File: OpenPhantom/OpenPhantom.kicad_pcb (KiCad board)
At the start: 2 copper layers, 175 x 175 mm, 110 parts, among them J1 Barrel_Jack, J2 Video, J3 Audio, Q1 BC548, Q2 BD136, Q3 BC557, Q4 BC548, SW1 POWER, SW2 RESET, U1 UM6116 VRAM, U10 74HC368, U11 74HC368, U2 UM6116 WRAM, U3 74HC04, U4 UA6547_CPU, U5 4013, U6 UA6548_PPU, U7 74HC139, U8 74LS373, U9 LM7805, Y1 21.453366 MHz

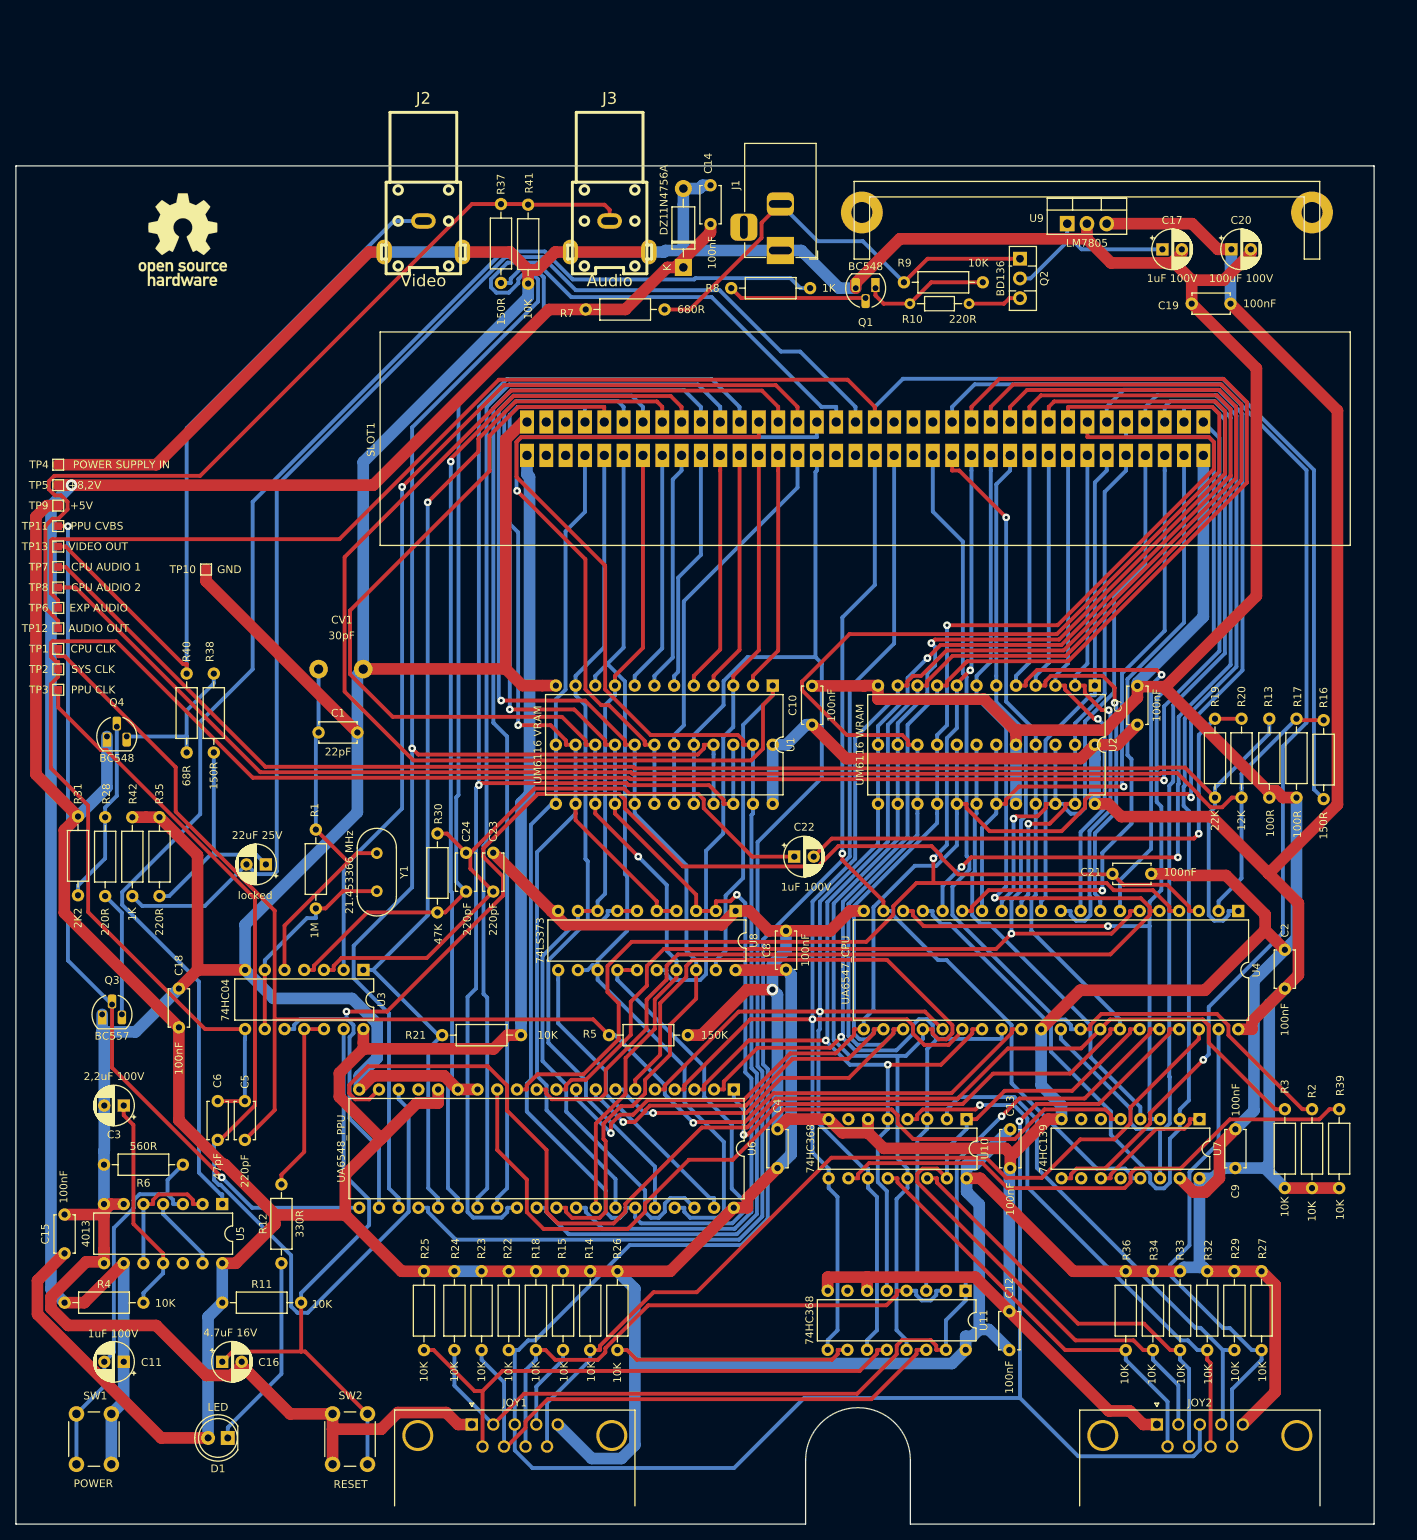
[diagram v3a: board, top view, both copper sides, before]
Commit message: Fixed Routes
Power route fix.
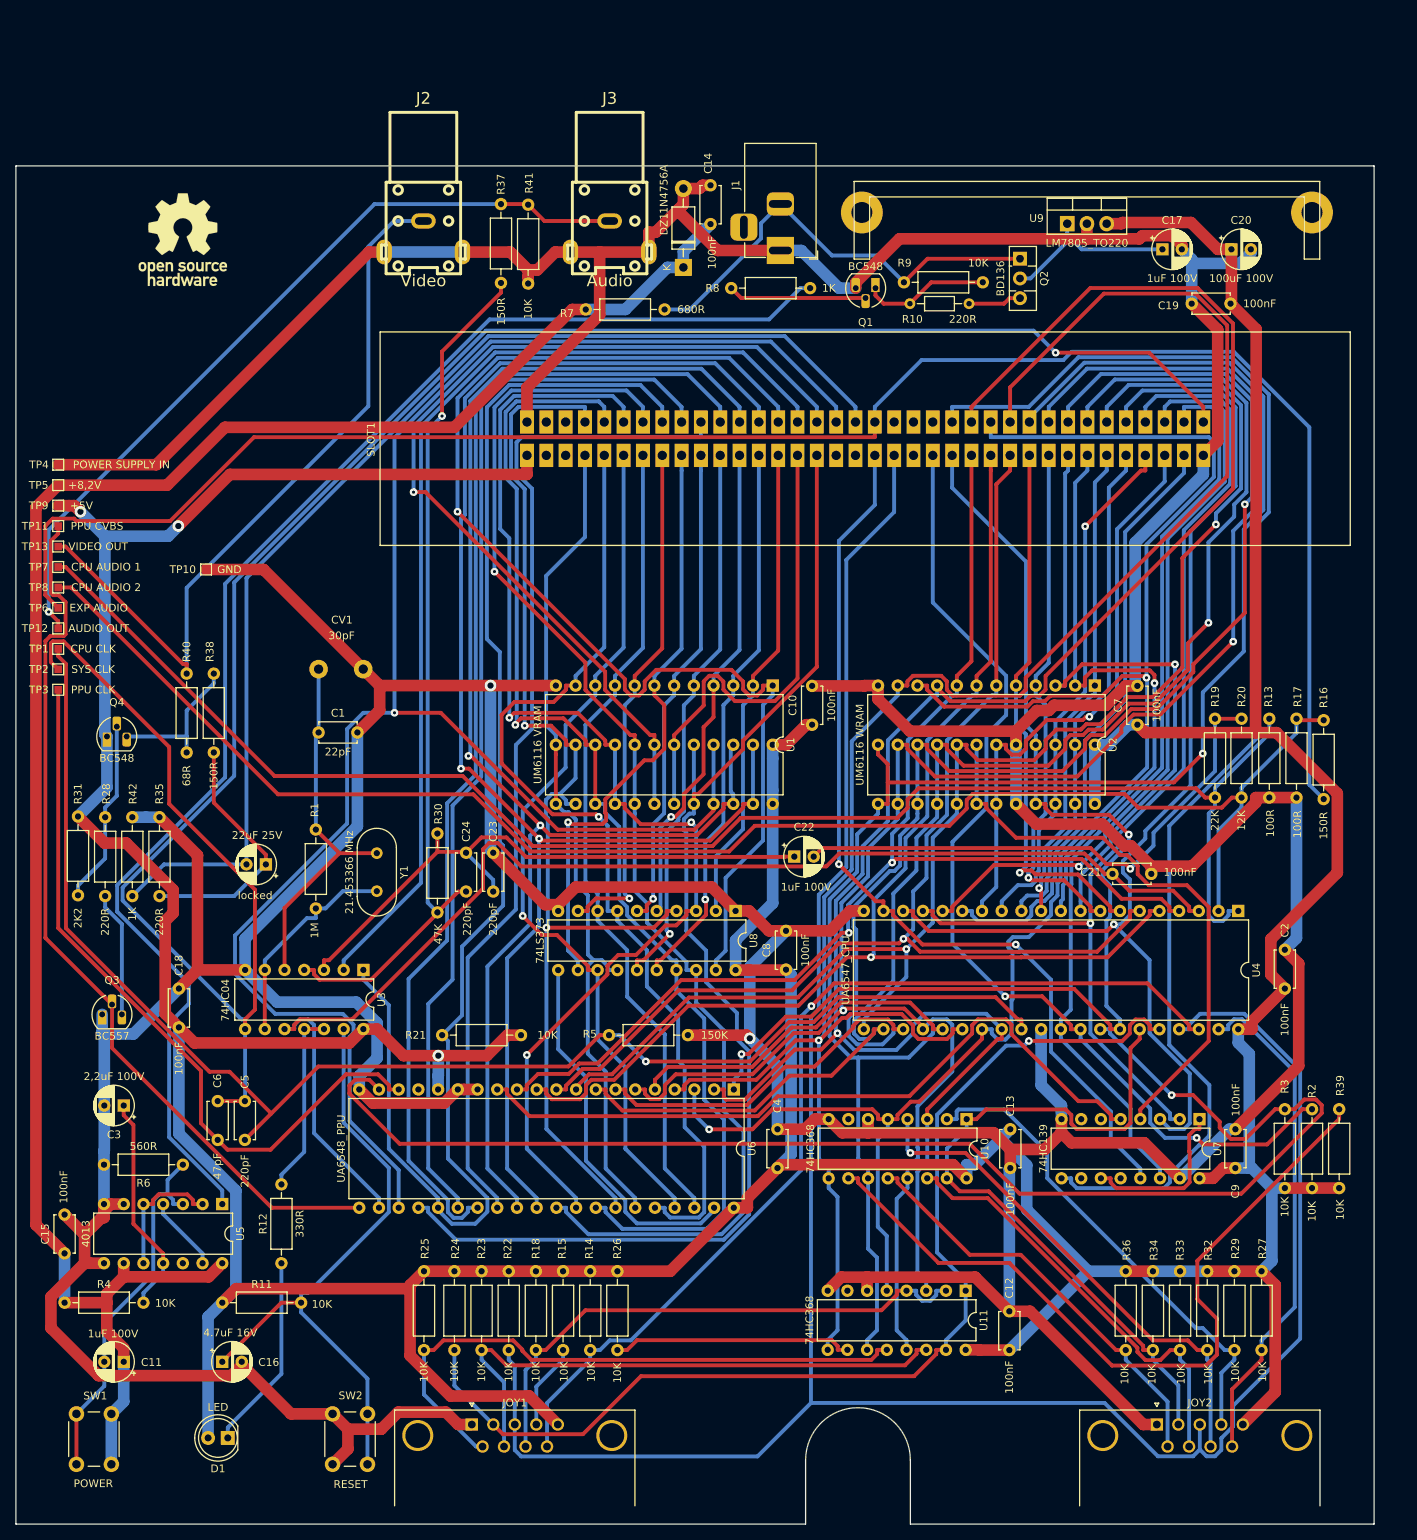
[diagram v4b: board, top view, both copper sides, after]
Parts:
- U9: value LM7805 -> LM7805_TO220
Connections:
- C15 pad 1: /VCC -> /+8,2V
- U5 pad 14: /VCC -> /+8,2V
- U8 pad 12: /PPU-D1 -> /PPU-A1
- U8 pad 15: /PPU-D3 -> /PPU-A3
- U8 pad 2: /PPU-D6 -> /PPU-A6
- U8 pad 5: /PPU-D4 -> /PPU-A4
- U8 pad 6: /PPU-D2 -> /PPU-A2
- U8 pad 9: /PPU-D0 -> /PPU-A0
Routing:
- net /VCC: track 899.1 -> 765.1 mm, vias 0 -> 3
- net /GND: track 1118.3 -> 1007.0 mm, vias 1 -> 2
- net /PPU-D3: track 166.9 -> 108.6 mm
- net /PPU-A1: track 31.1 -> 77.6 mm, vias 0 -> 1
- net /CPU-D3: track 228.0 -> 269.6 mm, vias 2 -> 1
- net /PPU-A13: track 139.0 -> 179.7 mm, vias 1 -> 0
- net /PPU-A3: track 31.1 -> 71.6 mm, vias 0 -> 1
- net /PPU-CLK: track 134.2 -> 95.5 mm
- net /PPU-A0: track 31.1 -> 67.0 mm, vias 0 -> 1
- net /PPU-A7: track 191.5 -> 158.4 mm, vias 0 -> 1
- net /PPU-A4: track 31.0 -> 63.4 mm, vias 0 -> 1
- net /PPU-A2: track 31.1 -> 62.8 mm, vias 0 -> 1
- net /PPU-A6: track 31.0 -> 62.0 mm
- net /CPU-A13: track 169.9 -> 141.1 mm, vias 0 -> 1
- net /4017-D2: track 70.6 -> 98.6 mm
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
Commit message: RCA Plug fix
Fixed RCA plug pinout
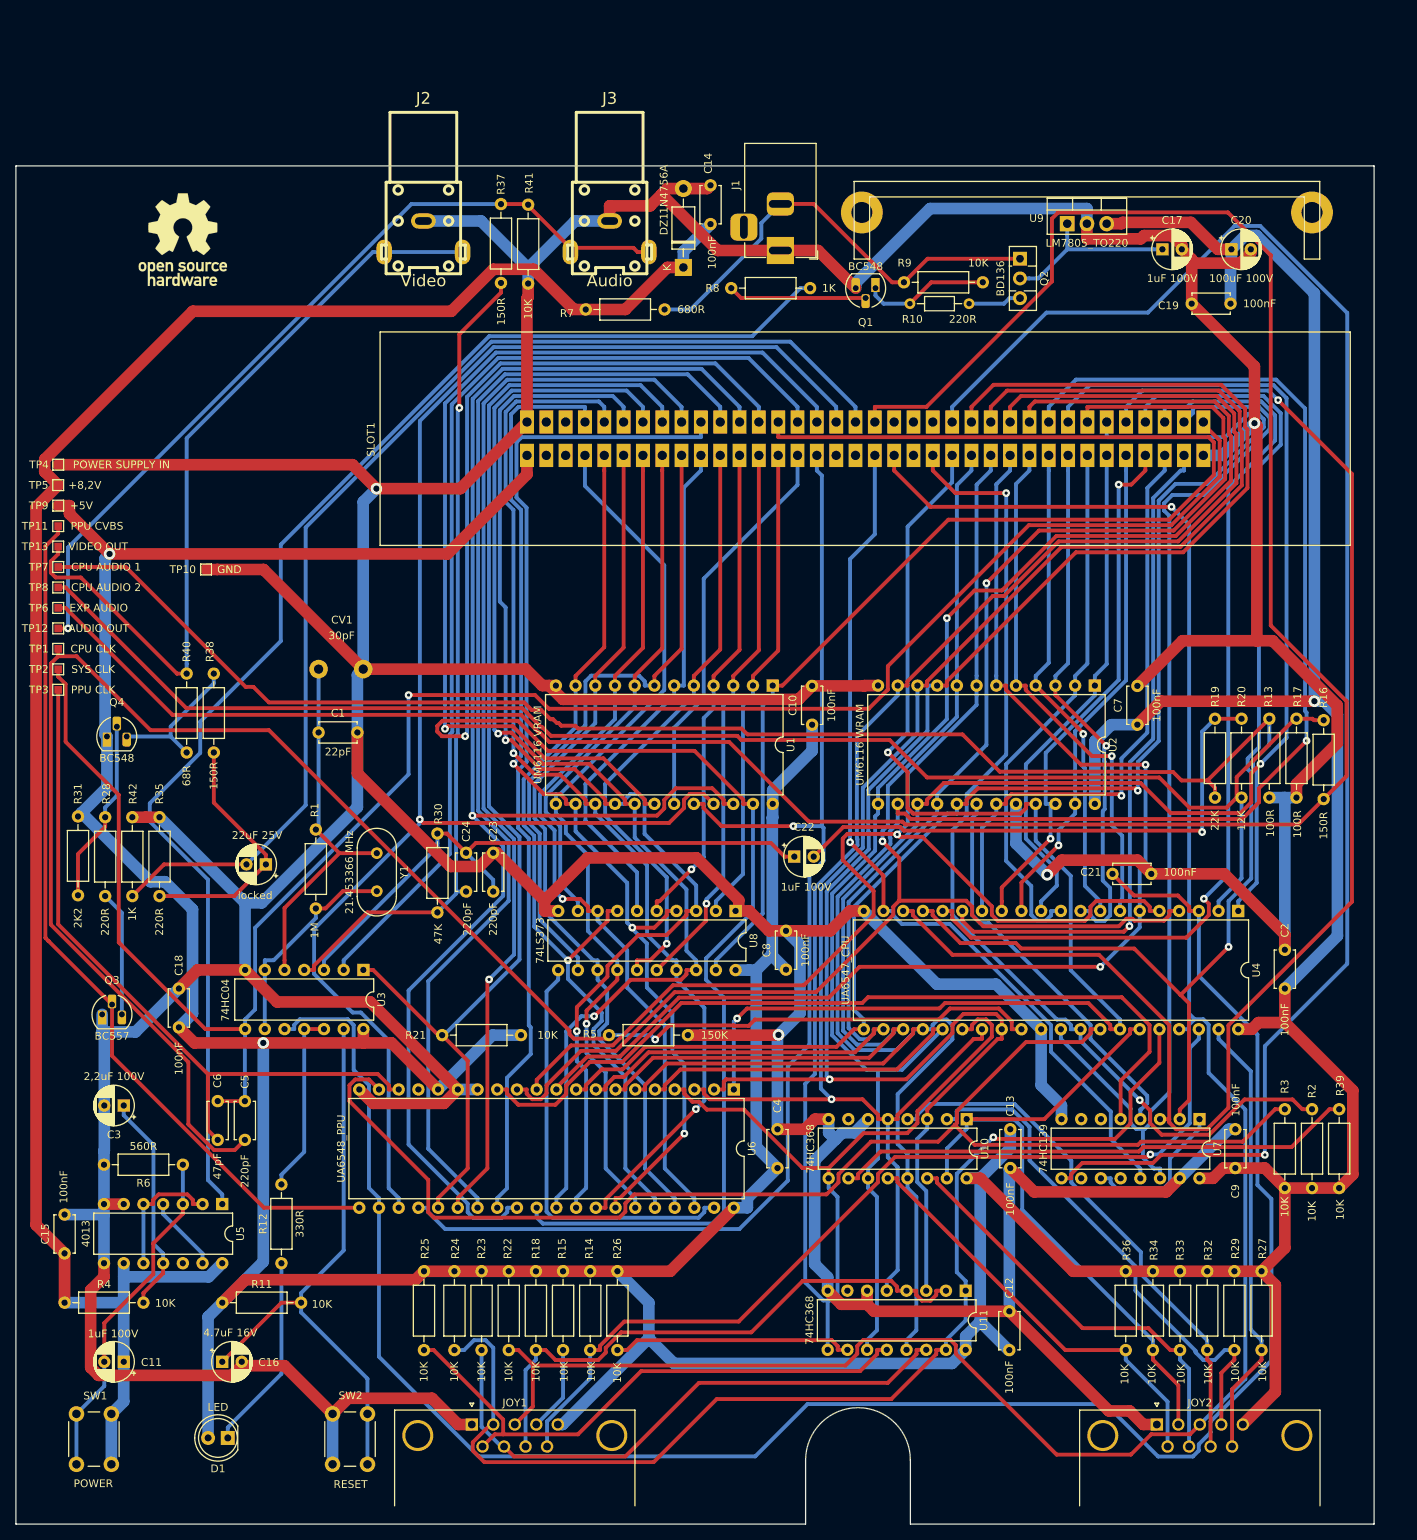
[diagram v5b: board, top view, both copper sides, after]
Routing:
- net /RST: track 168.3 -> 261.7 mm
- net /EXP-6: track 238.7 -> 321.7 mm
- net /GND: track 1007.0 -> 1084.1 mm, vias 2 -> 4
- net /SYSTEM-CLK: track 293.6 -> 251.2 mm
- net /CPU-CLK: track 185.7 -> 226.8 mm
- net /VCC: track 765.1 -> 805.8 mm
- net /EXP-1: track 314.0 -> 276.6 mm, vias 0 -> 1
- net /~{ROMSEL}: track 173.6 -> 207.8 mm, vias 0 -> 1
- net /PPU-~{WE}: track 248.7 -> 215.6 mm
- net /CPU-A14: track 155.4 -> 188.2 mm
- net /CPU-D3: track 269.6 -> 237.8 mm
- net /4017-D2: track 98.6 -> 67.2 mm
- net /CPU-D4: track 250.0 -> 278.6 mm, vias 2 -> 1
- net /PPU-A13: track 179.7 -> 152.4 mm
- net /PPU-A8: track 194.1 -> 220.1 mm, vias 2 -> 1
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
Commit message: Added C26 + RF circuit removed
Added C26 removed RF circuit components fixing audio noise.
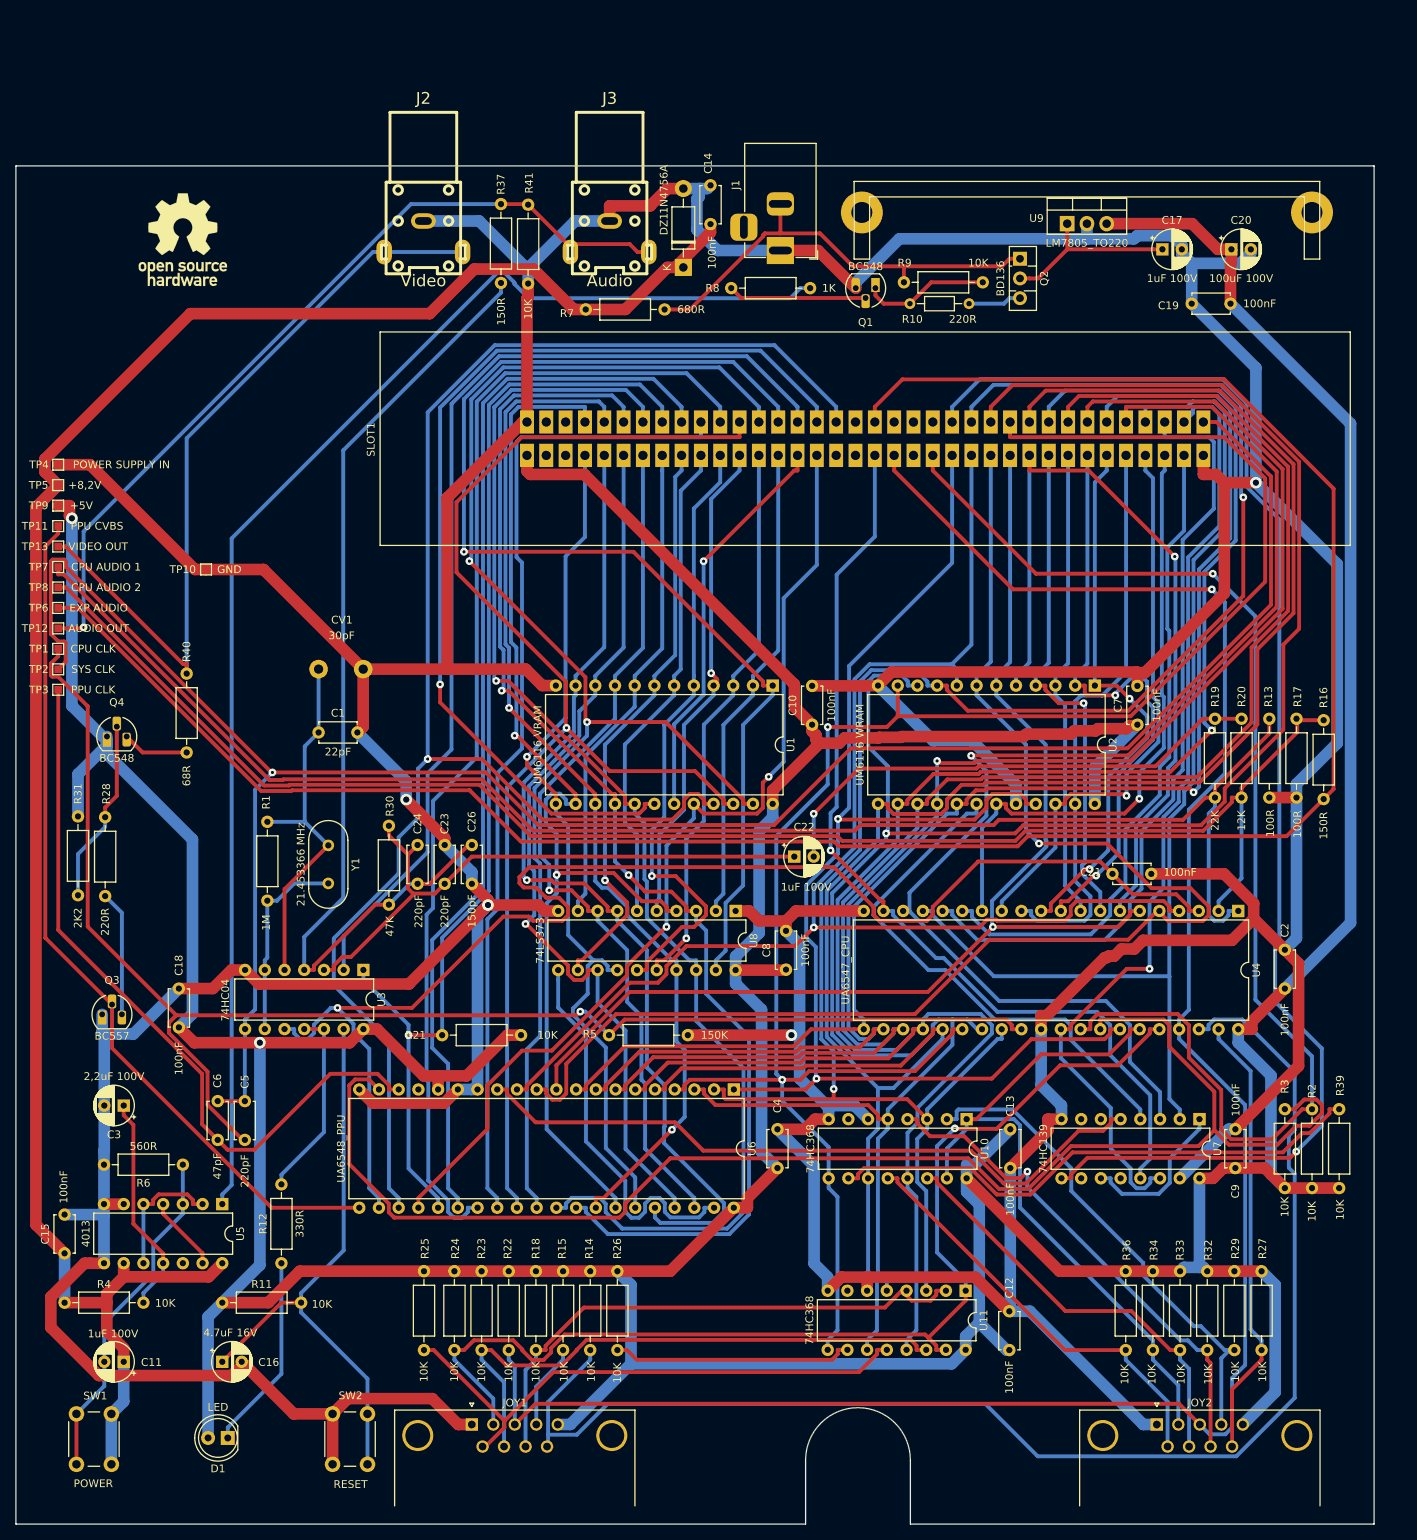
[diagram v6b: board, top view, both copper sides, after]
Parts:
- removed R35: 220R, Resistor_THT:R_Axial_DIN0207_L6.3mm_D2.5mm_P10.16mm_Horizontal
- removed R38: 150R, Resistor_THT:R_Axial_DIN0207_L6.3mm_D2.5mm_P10.16mm_Horizontal
- removed R42: 1K, Resistor_THT:R_Axial_DIN0207_L6.3mm_D2.5mm_P10.16mm_Horizontal
- removed locked: 22uF 25V, Capacitor_THT:CP_Radial_D5.0mm_P2.50mm
- added C26: 150pF, Capacitor_THT:C_Disc_D4.7mm_W2.5mm_P5.00mm, F.Cu at (75.2, 113.5)
- moved C23 6.33 mm to (71.8, 118.5)
- moved C24 6.33 mm to (68.2, 118.5)
- moved R1 6.33 mm to (48.9, 110.5)
- moved R30 6.33 mm to (64.6, 121.2)
- moved Y1 6.33 mm to (56.8, 113.5)
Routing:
- net /EXP-5: track 149.2 -> 0.00 mm
- net /RST: track 261.7 -> 180.7 mm, vias 0 -> 1
- net /CPU-D1: track 225.8 -> 287.1 mm
- net /OUT-1: track 117.6 -> 177.1 mm, vias 1 -> 0
- net /GND: track 1084.1 -> 1028.7 mm
- net /CPU-CLK: track 226.8 -> 187.4 mm
- net /PPU-~{RD}: track 165.4 -> 127.0 mm, vias 1 -> 2
- net /CPU-A3: track 67.4 -> 104.3 mm
- net /PPU-A8: track 220.1 -> 183.8 mm, vias 1 -> 2
- net /EXP-6: track 321.7 -> 287.3 mm
- net Net-(C25-Pad1): track 32.6 -> 0.00 mm
- net /~{ROMSEL}: track 207.8 -> 176.9 mm
- net /PPU-A9: track 199.0 -> 168.2 mm
- net /~{IRQ}: track 132.5 -> 162.8 mm, vias 2 -> 1
- net /CPU-A14: track 188.2 -> 163.6 mm
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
